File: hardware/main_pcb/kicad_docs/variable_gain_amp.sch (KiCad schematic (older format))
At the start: 8 parts, among them U1 MCP6002-xP

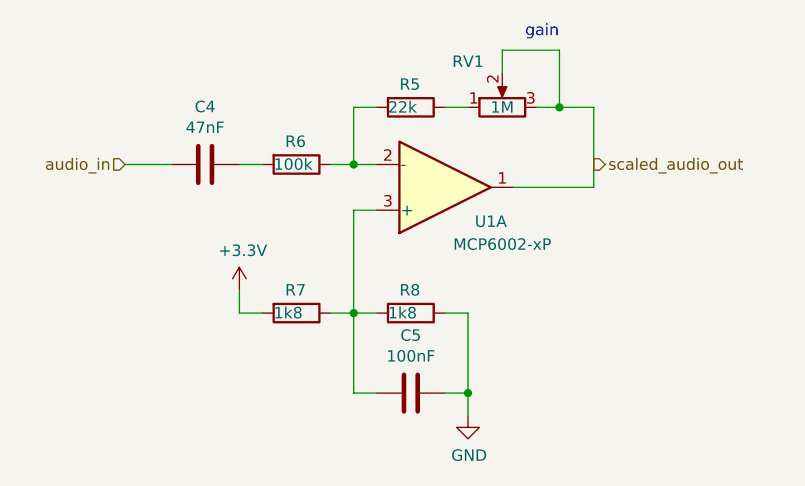
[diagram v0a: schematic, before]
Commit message: change gain pot to 100k
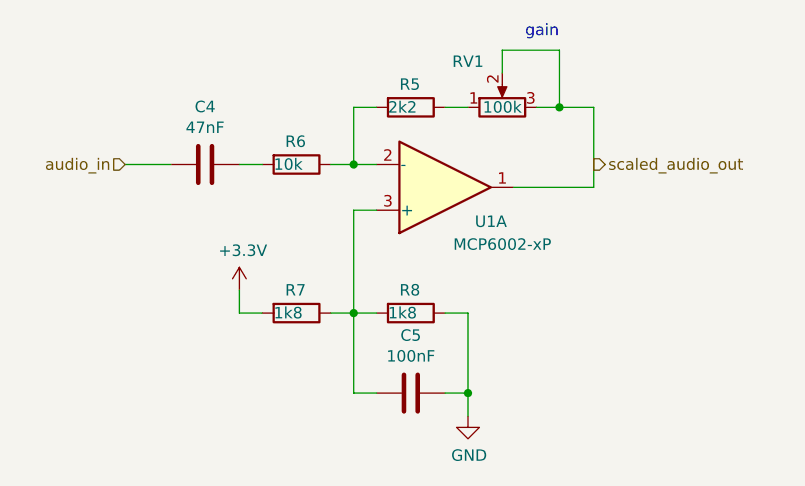
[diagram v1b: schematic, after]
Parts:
- R5: value 22k -> 2k2
- R6: value 100k -> 10k
- RV1: value 1M -> 100k
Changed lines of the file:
@@
 AR Path="/5F122414/5F1F7EDD" Ref="R6"  Part="1"
 F 0 "R6" V 5150 3500 50  0000 L CNN
-F 1 "100k" V 5250 3450 50  0000 L CNN
+F 1 "10k" V 5250 3450 50  0000 L CNN
 F 2 "Resistor_SMD:R_0805_2012Metric_Pad1.15x1.40mm_HandSolder" V 5180 3550 50  0001 C CNN
 F 3 "~" H 5250 3550 50  0001 C CNN
@@
 P 6150 3300
 F 0 "RV1" V 6350 3450 50  0000 C CNN
-F 1 "1M" V 6150 3300 50  0000 C CNN
+F 1 "100k" V 6150 3300 50  0000 C CNN
 F 2 "Potentiometer_THT:Potentiometer_Alpha_RD901F-40-00D_Single_Vertical" H 6150 3300 50  0001 C CNN
 F 3 "~" H 6150 3300 50  0001 C CNN
@@
 Text Notes 6250 3000 0    50   ~ 0
 gain
+Wire Wire Line
+	5900 3300 6000 3300
+Wire Wire Line
+	5600 3300 5500 3300
+Wire Wire Line
+	4500 3550 4700 3550
 $Comp
 L Device:R R?
@@
 AR Path="/5F122414/5F3ABCDA" Ref="R5"  Part="1"
 F 0 "R5" V 5650 3250 50  0000 L CNN
-F 1 "22k" V 5750 3200 50  0000 L CNN
+F 1 "2k2" V 5750 3200 50  0000 L CNN
 F 2 "Resistor_SMD:R_0805_2012Metric_Pad1.15x1.40mm_HandSolder" V 5680 3300 50  0001 C CNN
 F 3 "~" H 5750 3300 50  0001 C CNN
@@
 	0    1    1    0
 $EndComp
-Wire Wire Line
-	5900 3300 6000 3300
-Wire Wire Line
-	5600 3300 5500 3300
-Wire Wire Line
-	4500 3550 4700 3550
 $EndSCHEMATC

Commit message: rev 1.1, fix silkscreen, flip trimpots, adjust hpf
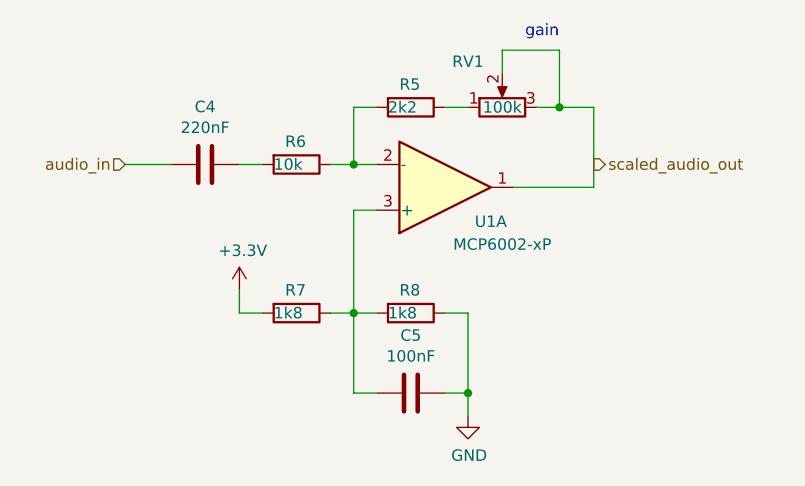
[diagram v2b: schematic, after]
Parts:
- C4: value 47nF -> 220nF
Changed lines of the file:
@@
 P 4850 3550
 F 0 "C4" V 4598 3550 50  0000 C CNN
-F 1 "47nF" V 4689 3550 50  0000 C CNN
+F 1 "220nF" V 4689 3550 50  0000 C CNN
 F 2 "Capacitor_SMD:C_0805_2012Metric_Pad1.15x1.40mm_HandSolder" H 4888 3400 50  0001 C CNN
 F 3 "~" H 4850 3550 50  0001 C CNN
